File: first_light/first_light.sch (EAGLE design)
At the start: 50 parts, among them IC1 MC34063AD, J1 DCJ0202, J2 DCJ0202, Q1 ZXMN4A06GTA, U1 ESP32-WROOM-32D

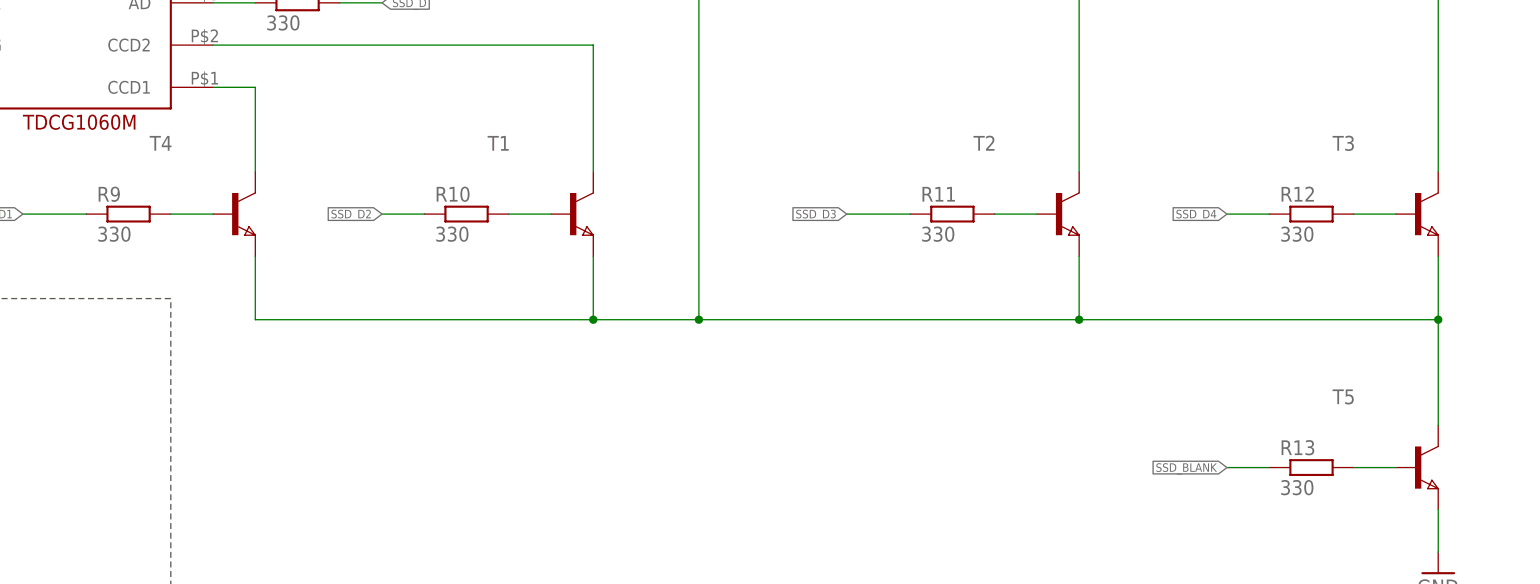
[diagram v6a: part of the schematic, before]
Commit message: board designator positioning
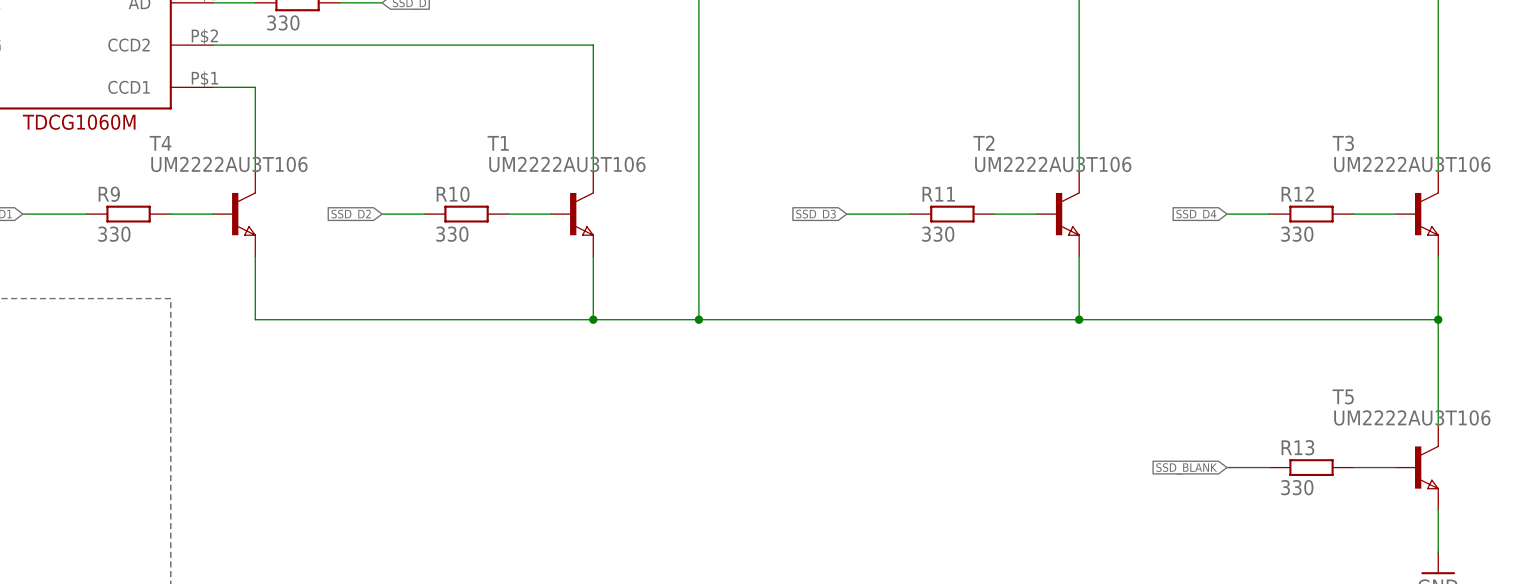
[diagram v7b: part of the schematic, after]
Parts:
- T1, T2, T3, T4, T5: value (none) -> UM2222AU3T106
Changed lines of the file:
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@@
 <part name="R7" library="rcl" library_urn="urn:adsk.eagle:library:334" deviceset="R-EU_" device="R0603" package3d_urn="urn:adsk.eagle:package:23555/3" value="330"/>
 <part name="R8" library="rcl" library_urn="urn:adsk.eagle:library:334" deviceset="R-EU_" device="R0603" package3d_urn="urn:adsk.eagle:package:23555/3" value="330"/>
-<part name="T1" library="zetex" library_urn="urn:adsk.eagle:library:418" deviceset="NPNSOT323" device="" package3d_urn="urn:adsk.eagle:package:30986/2"/>
-<part name="T2" library="zetex" library_urn="urn:adsk.eagle:library:418" deviceset="NPNSOT323" device="" package3d_urn="urn:adsk.eagle:package:30986/2"/>
-<part name="T3" library="zetex" library_urn="urn:adsk.eagle:library:418" deviceset="NPNSOT323" device="" package3d_urn="urn:adsk.eagle:package:30986/2"/>
-<part name="T4" library="zetex" library_urn="urn:adsk.eagle:library:418" deviceset="NPNSOT323" device="" package3d_urn="urn:adsk.eagle:package:30986/2"/>
-<part name="T5" library="zetex" library_urn="urn:adsk.eagle:library:418" deviceset="NPNSOT323" device="" package3d_urn="urn:adsk.eagle:package:30986/2"/>
+<part name="T1" library="zetex" library_urn="urn:adsk.eagle:library:418" deviceset="NPNSOT323" device="" package3d_urn="urn:adsk.eagle:package:30986/2" value="UM2222AU3T106"/>
+<part name="T2" library="zetex" library_urn="urn:adsk.eagle:library:418" deviceset="NPNSOT323" device="" package3d_urn="urn:adsk.eagle:package:30986/2" value="UM2222AU3T106"/>
+<part name="T3" library="zetex" library_urn="urn:adsk.eagle:library:418" deviceset="NPNSOT323" device="" package3d_urn="urn:adsk.eagle:package:30986/2" value="UM2222AU3T106"/>
+<part name="T4" library="zetex" library_urn="urn:adsk.eagle:library:418" deviceset="NPNSOT323" device="" package3d_urn="urn:adsk.eagle:package:30986/2" value="UM2222AU3T106"/>
+<part name="T5" library="zetex" library_urn="urn:adsk.eagle:library:418" deviceset="NPNSOT323" device="" package3d_urn="urn:adsk.eagle:package:30986/2" value="UM2222AU3T106"/>
 <part name="R9" library="rcl" library_urn="urn:adsk.eagle:library:334" deviceset="R-EU_" device="R0603" package3d_urn="urn:adsk.eagle:package:23555/3" value="330"/>
 <part name="R10" library="rcl" library_urn="urn:adsk.eagle:library:334" deviceset="R-EU_" device="R0603" package3d_urn="urn:adsk.eagle:package:23555/3" value="330"/>

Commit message: added MFPN and DKPN for all parts + exported BOM
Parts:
- C3, C4, C5: DKPN (none) -> 1276-1935-1-ND; MFPN (none) -> CL10B104KB8NNWC
- C6: value 470uF -> 680uF; DKPN (none) -> 565-5128-1-ND; MFPN (none) -> EMZR6R3ARA681MF80G
- C7: DKPN (none) -> 1276-1094-1-ND; MFPN (none) -> CL10B471KB8NNNC
- C8: DKPN (none) -> 2616-VE-101M1CTR-0605S-ND; MFPN (none) -> VE-101M1CTR-0605S
- D1: DKPN (none) -> 1N5819HW-FDICT-ND; MFPN (none) -> 1N5819HW-7-F
- F1: DKPN (none) -> 507-1776-1-ND; MFPN (none) -> 0ZCG0160BF2C
- IC1: DKPN (none) -> MC34063ADR2GOSCT-ND; MFPN (none) -> MC34063ADR2G
- J1, J2: DKPN (none) -> 2092-KLDX-0202-BC-ND; MFPN (none) -> KLDX-0202-BC
- LED1: value ALM -> GREEN; DKPN (none) -> 732-4980-1-ND; MFPN (none) -> 150060VS75000
- LED2: value SET -> GREEN; DKPN (none) -> 732-4980-1-ND; MFPN (none) -> 150060VS75000
- Q1: DKPN (none) -> ZXMN4A06GCT-ND; MFPN (none) -> ZXMN4A06GTA
- R1, R10, R11, R12, R13, R17, R18, R2, R3, R4, R5, R6, R7, R8, R9: value 330 -> 330R; DKPN (none) -> 311-330GRCT-ND; MFPN (none) -> RC0603JR-07330RL
- R14: DKPN (none) -> 311-100GRCT-ND; MFPN (none) -> RC0603JR-07100RL
- R15, R21, R22, R23: DKPN (none) -> 13-RC0603JR-1010KLCT-ND; MFPN (none) -> RC0603JR-1010KL
- R19: DKPN (none) -> P17485CT-ND; MFPN (none) -> ERJ-3BWJR033V
- R20: DKPN (none) -> 311-8.2KGRCT-ND; MFPN (none) -> RC0603JR-078K2L
- S_DOWN: value DOWN -> tact; DKPN (none) -> 2223-TS02-66-60-BK-100-LCR-D-ND; MFPN (none) -> TS02-66-60-BK-100-LCR-D
- S_LEFT: value LEFT -> tact; DKPN (none) -> 2223-TS02-66-60-BK-100-LCR-D-ND; MFPN (none) -> TS02-66-60-BK-100-LCR-D
- S_RIGHT: value RIGHT -> tact; DKPN (none) -> 2223-TS02-66-60-BK-100-LCR-D-ND; MFPN (none) -> TS02-66-60-BK-100-LCR-D
- S_RST: DKPN (none) -> 2223-TS02-66-60-BK-100-LCR-D-ND; MFPN (none) -> TS02-66-60-BK-100-LCR-D
- S_UP: value UP -> tact; DKPN (none) -> 2223-TS02-66-60-BK-100-LCR-D-ND; MFPN (none) -> TS02-66-60-BK-100-LCR-D
- T1, T2, T3, T4, T5: DKPN (none) -> 846-UM2222AU3T106CT-ND; MFPN (none) -> UM2222AU3T106
- U$1: DKPN (none) -> TDCG1060M-ND; MFPN (none) -> TDCG1060M
- U$2: DKPN (none) -> 732-4110-1-ND; MFPN (none) -> 7447714221
- U1: DKPN (none) -> 1965-ESP32-WROOM-32E-H4CT-ND; MFPN (none) -> ESP32-WROOM-32E-H4
- renumbered S1 to S_RST, S2 to S_UP, S3 to S_DOWN, S4 to S_LEFT, S5 to S_RIGHT
